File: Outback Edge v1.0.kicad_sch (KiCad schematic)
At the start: 19 parts, among them J1 USB_C_Receptacle_USB2.0_16P, J2 OE_M.2_Socket_E, J3 RJ45_LED_Shielded, J4 Micro_SD_Card_Det_Hirose_DM3AT, J5 USB3_A_Stacked, SW1 SW_Push, U1 R7FA6M5AH3CFB#AA0, U2 USB2514B_Bi

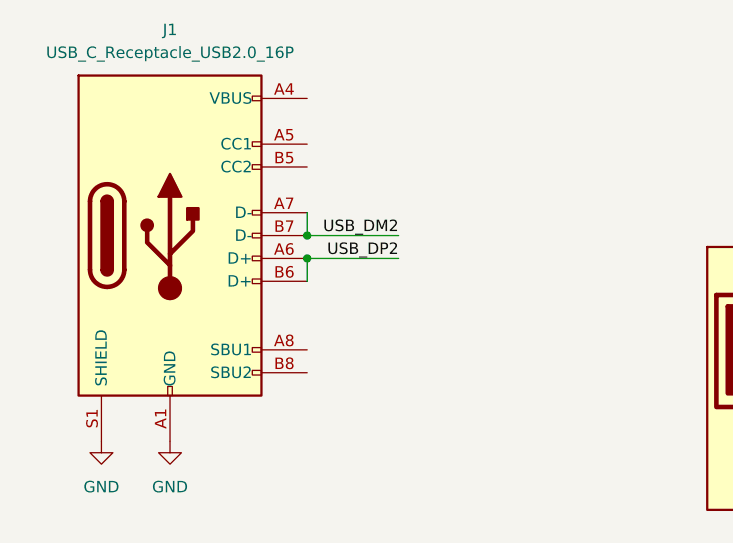
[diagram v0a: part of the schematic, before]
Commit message: Add USB-C CC pull-down resistors
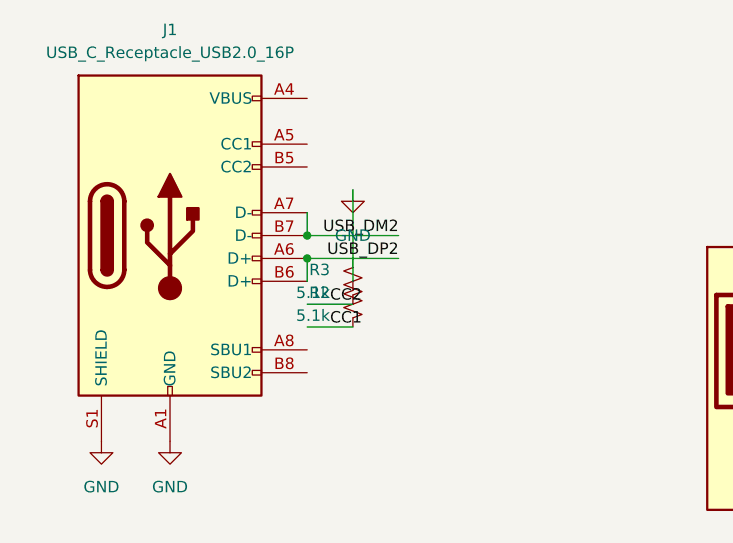
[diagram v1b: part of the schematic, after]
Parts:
- added R2, R3: 5.1k, Resistor_SMD:R_0402_1005Metric, symbol Device:R_Small_US
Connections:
- net GND: now also R2.2, R3.2
- new net CC1: R2.1
- new net CC2: R3.1
